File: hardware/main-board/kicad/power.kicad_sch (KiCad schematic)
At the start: 51 parts, among them J101 PANEL_USB, J102 BATTERY, Q101 AO3400A, Q102 AO3401A, Q103 AO3400A, U101 USBLC6-2SC6, U102 BQ25798RQMR, U103 MAX17048G+T10, U105 TPS62903RPJR

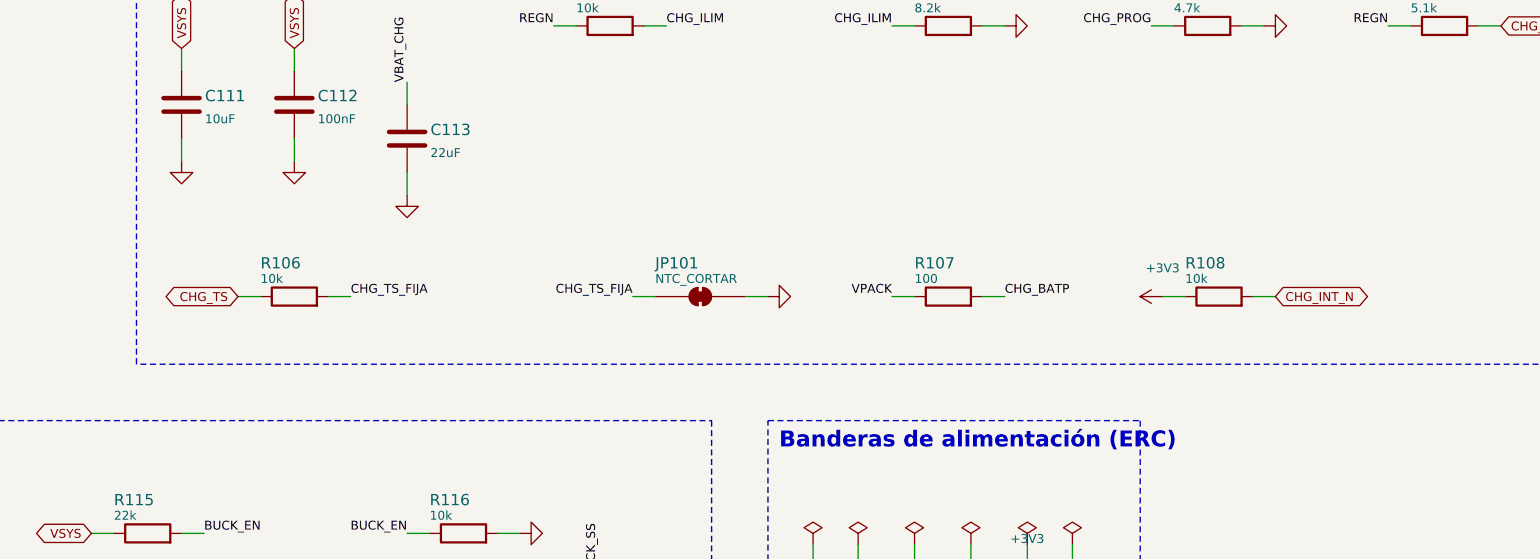
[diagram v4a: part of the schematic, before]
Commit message: Placa principal v0.2: NTC de la celda obligatoria en J404
- Fuera R106 (10k fijo) y el puente JP101: TS siempre ve la NTC. Sin NTC enchufada no carga;
  el sistema sigue encendido con el USB.
- Con el divisor 5.1k/30k y una NTC 10k B3435 (103AT), umbrales por omisión del BQ25798 (hoja
  de datos, VT1/TS_COOL/TS_WARM/VT5): no carga bajo ~2 ni sobre ~61 grados, 20 % de corriente
  entre ~2 y 11 y 400 mV menos de voltaje entre ~45 y 61.
- El número R106 queda reservado para no renumerar las demás resistencias.
- README: tabla de temperaturas, aviso de no usar NTC de 100k de impresora 3D y cómo va la NTC
  pegada a la celda en la carcasa V2.3.
- 126 de 126 conexiones; DRC 0, sin conectar 0 y paridad en la placa, la panel-usb y el panel;
  ERC 0. Costo estimado 209.08 USD por 5 juegos.
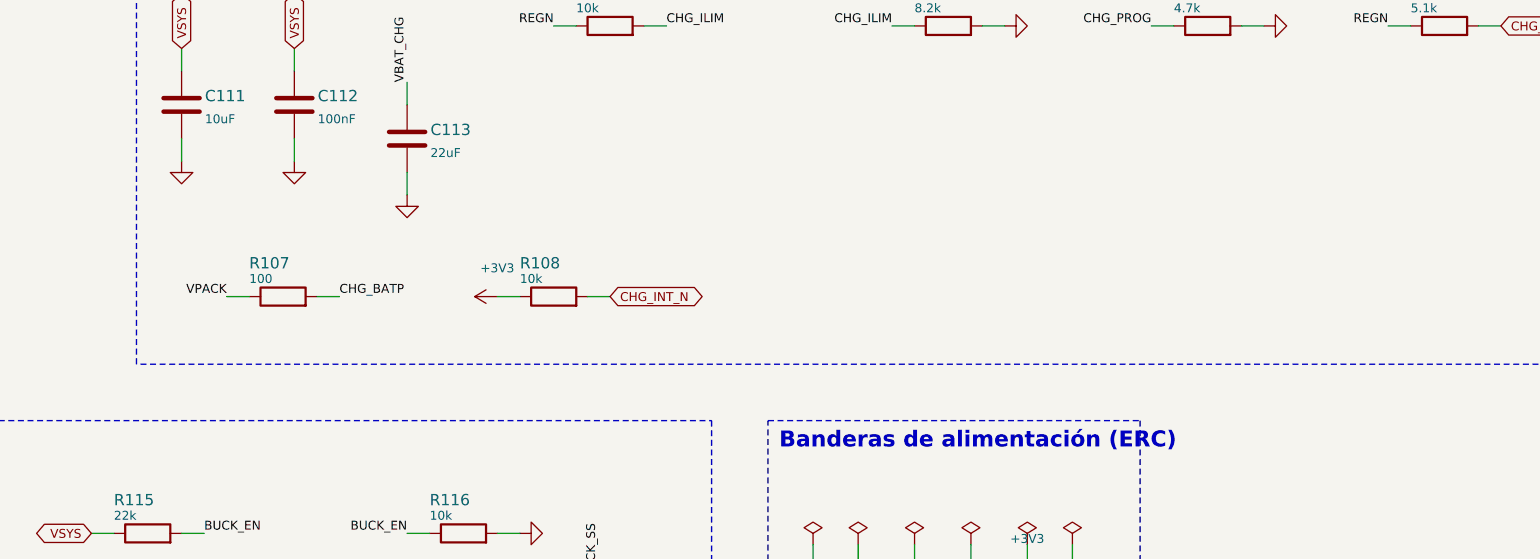
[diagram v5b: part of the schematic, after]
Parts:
- removed JP101: NTC_CORTAR, tresvizo_lcsc:SolderJumper-2_P1.3mm_Bridged_RoundedPad1.0x1.5mm, symbol Jumper:SolderJumper_2_Bridged
- removed R106: 10k, Resistor_SMD:R_0402_1005Metric, symbol Device:R
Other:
- moved on the sheet: R107, R108

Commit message: Placa principal v0.3 compacta: 36 × 71.5 mm para el tubo de Ø52, con USB-C, OLED, botón, LED y BMI088 en la placa
- Rama exploratoria pedida por el propietario el 07-10-2026. Especificación, interfaces con la
  carcasa, colocación y auditoría en research/v03-compacta.md.
- Esquema (ERC 0):
  - USB-C TYPE-C-31-M-12 con Rd de 5.1k, TVS SMF15A y USBLC6;
  - pulsador TS-1187A a BTN_N;
  - LED de estado en GPIO48 con 330 Ω;
  - OLED del propietario soldada sobre pads SMD (J403);
  - BMI088 por I2C (GPIO41/42, INT1 en GPIO2 e INT3 en GPIO1);
  - J102 en GH 4, con dos contactos por polo;
  - TP208 y TP209 en la UART0.
  Fuera J402, J405 y Q402; la panel-usb ya no se usa.
- Placa de 4 capas con muescas para la funda del USB-C y para la clavija SMA de la carrier.
  - Los bloques del cargador y de los reguladores se mueven sin cambiar su geometría interna.
  - La antena del WROOM va hacia −X, con zona sin cobre.
  - Panel de una sola placa.
  - DRC con 0 violaciones, 0 sin conectar y 0 de paridad; el panel, igual.
- Auditoría eléctrica independiente (08-10-2026), con sus siete puntos corregidos:
  - las soldaduras de la OLED ya no quedan frente al SMA de la carrier;
  - puentes del panel lejos del IMU y de los condensadores de potencia;
  - zona sin cobre de la antena más grande;
  - GND de J102 y vías dobles en VPACK;
  - vías junto al pad de tierra del WROOM;
  - LED más brillante;
  - pads de la UART.
- cad/export_board_step.py exporta el STEP en los ejes de la carcasa, con los modelos de LCSC
  corregidos. cad/check_heights.py comprueba los altos contra el tubo: todas las piezas caben con
  0.3 mm de aire.
- Cambios en los scripts:
  - route_rest.py admite límites de búsqueda por entorno;
  - fanout.py respeta las vías prerruteadas;
  - finish_pcb.py --final quita las vías sin uso;
  - cost_jlc.py sirve para una sola placa.
- Costo estimado en JLCPCB: 236.43 USD por 5 placas montadas, sin el PCB ni el envío.
- El build casi siempre se repite igual. En una de cuatro corrid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
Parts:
- added R119, R120: 5.1k, Resistor_SMD:R_0402_1005Metric, symbol Device:R
- J101: value PANEL_USB -> USB_C; footprint tresvizo_lcsc:CONN-SMD_8P-P1.25_XUNPU-WAFER-GH1.25-8PWB -> tresvizo_lcsc:USB-C_SMD-TYPE-C-31-M-12; symbol Connector_Generic_MountingPin:Conn_01x08_MountingPin -> Connector:USB_C_Receptacle_USB2.0_16P; LCSC C3029383 -> C165948; MPN WAFER-GH1.25-8PWB -> TYPE-C-31-M-12
- J102: footprint tresvizo_lcsc:CONN-SMD_P2.00_S2B-PH-SM4-TB-LF-SN -> tresvizo_lcsc:CONN-SMD_4P-P1.25_SM04B-GHS-TB-LF-SN; symbol Connector_Generic_MountingPin:Conn_01x02_MountingPin -> Connector_Generic_MountingPin:Conn_01x04_MountingPin; LCSC C295747 -> C189895; MPN S2B-PH-SM4-TB(LF)(SN) -> SM04B-GHS-TB(LF)(SN)
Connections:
- net GND: now also J101.A1 (GND), J101.A12 (GND), J101.B1 (GND), J101.B12 (GND), J101.SH (SHIELD), J102.2 (Pin_2), R119.2, R120.2; no longer J101.4 (Pin_4), J101.5 (Pin_5), J101.6 (Pin_6), J101.MP (MountPin)
- net USB_DN: now also J101.A7 (D-), J101.B7 (D-); no longer J101.7 (Pin_7)
- net USB_DP: now also J101.A6 (D+), J101.B6 (D+); no longer J101.8 (Pin_8)
- net VBATT_IN: now also J102.3 (Pin_3), J102.4 (Pin_4); no longer J102.2 (Pin_2)
- net VBUS: now also J101.A4 (VBUS), J101.A9 (VBUS), J101.B4 (VBUS), J101.B9 (VBUS); no longer J101.1 (Pin_1), J101.2 (Pin_2), J101.3 (Pin_3)
- new net CC1: J101.A5 (CC1), R119.1
- new net CC2: J101.B5 (CC2), R120.1
- no-connect marks 4 -> 6
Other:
- note added: "Entrada USB-C (5 V sin PD, datos al ESP32)"
- note added: "J102 (GH 4, dos contactos por polo): el pack necesita cable GH de 4 hilos AWG 26; ICHG del BQ25798 <= 1.5 A."
- note removed: "Entrada USB-C del panel (5 V, datos al ESP32)"
- moved on the sheet: C101, C102, C103, C104, C105, C106, C107, C108, C109, C110, C111, C112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

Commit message: v0.3: endurecimiento de la placa y de la carcasa V3.0 (Ø56 × 111)
Carcasa V3.0:
- Tubo de Ø56 × 111 con pared de 2.4 (antes Ø52 × 100). Holguras, en la posición final y en los
  11 barridos de montaje:
  - 0.4 mm en los ajustes entre piezas impresas;
  - 0.25 por cara en los rieles de la placa;
  - 0.5 de aire a todo lo comprado.
  El coaxial va con curvas de R 10. La placa no cambió de sitio; la carrier va 0.1 más atrás.
- Antena:
  - SMA hembra de panel al centro de la tapa para la HA-901A. La tienda da conector macho
    («SMA-J»); si resulta hembra, un parámetro cambia la tapa a un paso de 12 mm.
  - Coaxial RG 178 B/U de unos 75 mm, con SMA macho acodado en la carrier.
  - Arandelas ISO 7092 en los tornillos de la antena.
- Correcciones de la revisión externa:
  - eje real de la tarjeta microSD (z 40.9), tomado de J401 y no de la ranura;
  - arnés real de la batería y la NTC, con su recorrido;
  - procedimiento de desarmado completo.
- Tapa de TPU amarrada para el USB-C y la microSD, logo en relieve de 0.5 al frente y líneas
  verticales decorativas atrás, como en V2.3.
- check_v3_0.py: 0 choques y guarda de pared sin faltantes. Se cumplen los objetivos de holgura; la
  pared más delgada mide 1.198 mm, en una unión.

Placa v0.3, sin mover piezas:
- C104, C106 y C107 pasan de 22 a 10 µF (C15850). La carga que pide el USB al enchufar baja de unos
  259 a 118 µC. Sigue arriba de la regla de 10 µF de USB 2.0: queda como decisión del propietario.
- VSYS por In2.Cu a 1.2 mm y GNSS_5V a 0.6 mm, con más vías.
- Tabla de valores para el firmware: ICHG de 1.5 A como máximo, límite de entrada, reinicio con el
  botón, OLED girada 180° y ejes del IMU.
- ERC 0. DRC 0/0/0 y panel 0/0. Dos builds iguales byte a byte. 234.15 USD por 5 placas montadas.
- check_heights.py lee el tubo de la carcasa y mide 0.5 de aire en radio: todas las piezas caben.

Pendiente: confirmar el conector de la antena, medir la carrier y la OLED, y el orden de los pines
de la OLED.
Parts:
- C104, C106, C107: value 22uF -> 10uF; LCSC C45783 -> C15850; MPN CL21A226MAQNNNE -> CL21A106KAYNNNE
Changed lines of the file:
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@@
 			)
 		)
-		(property "Value" "22uF"
+		(property "Value" "10uF"
 			(at 294.732 40.97 0)
 			(effects
@@
 			)
 		)
-		(property "Description" "22uF 25V X5R"
+		(property "Description" "10uF 25V X5R"
 			(at 292.1 39.37 0)
 			(effects
@@
 			)
 		)
-		(property "MPN" "CL21A226MAQNNNE"
+		(property "MPN" "CL21A106KAYNNNE"
 			(at 292.1 39.37 0)
 			(effects
@@
 			)
 		)
-		(property "LCSC" "C45783"
+		(property "LCSC" "C15850"
 			(at 292.1 39.37 0)
 			(effects
@@
 			)
 		)
-		(property "Value" "22uF"
+		(property "Value" "10uF"
 			(at 320.132 40.97 0)
 			(effects
@@
 			)
 		)
-		(property "Description" "22uF 25V X5R"
+		(property "Description" "10uF 25V X5R"
 			(at 317.5 39.37 0)
 			(effects
@@
 			)
 		)
-		(property "MPN" "CL21A226MAQNNNE"
+		(property "MPN" "CL21A106KAYNNNE"
 			(at 317.5 39.37 0)
 			(effects
@@
 			)
 		)
-		(property "LCSC" "C45783"
+		(property "LCSC" "C15850"
 			(at 317.5 39.37 0)
 			(effects
@@
 			)
 		)
-		(property "Value" "22uF"
+		(property "Value" "10uF"
 			(at 332.832 40.97 0)
 			(effects
@@
 			)
 		)
-		(property "Description" "22uF 25V X5R"
+		(property "Description" "10uF 25V X5R"
 			(at 330.2 39.37 0)
 			(effects
@@
 			)
 		)
-		(property "MPN" "CL21A226MAQNNNE"
+		(property "MPN" "CL21A106KAYNNNE"
 			(at 330.2 39.37 0)
 			(effects
@@
 			)
 		)
-		(property "LCSC" "C45783"
+		(property "LCSC" "C15850"
 			(at 330.2 39.37 0)
 			(effects
